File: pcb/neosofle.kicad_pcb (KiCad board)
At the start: 2 copper layers, 140.2 x 120 mm, 68 parts, among them J1 JST_ACH_BM02B-ACHSS-GAN-ETF_S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, SW1 CPG135001S30, SW10 CPG135001S30, SW11 CPG135001S30, SW12 CPG135001S30, SW13 CPG135001S30, SW14 CPG135001S30, SW15 CPG135001S30, SW16 CPG135001S30, SW17 CPG135001S30, SW18 CPG135001S30, SW19 CPG135001S30, SW2 CPG135001S30, SW20 CPG135001S30, SW21 CPG135001S30, SW22 CPG135001S30, SW23 CPG135001S30, SW24 CPG135001S30, SW25 RotaryEncoder_Switch, SW26 CPG135001S30, SW27 CPG135001S30, SW28 CPG135001S30, SW29 CPG135001S30, SW3 CPG135001S30, SW30 CPG135001S30, SW4 CPG135001S30, SW5 CPG135001S30, SW6 CPG135001S30, SW7 CPG135001S30, SW8 CPG135001S30, SW9 CPG135001S30, U1 nice!nano v2

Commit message: Update 3D model references, enlarge pads to hand solder JST connector.
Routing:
- net BAT+: track 61.7 -> 65.1 mm, vias 2 -> 3

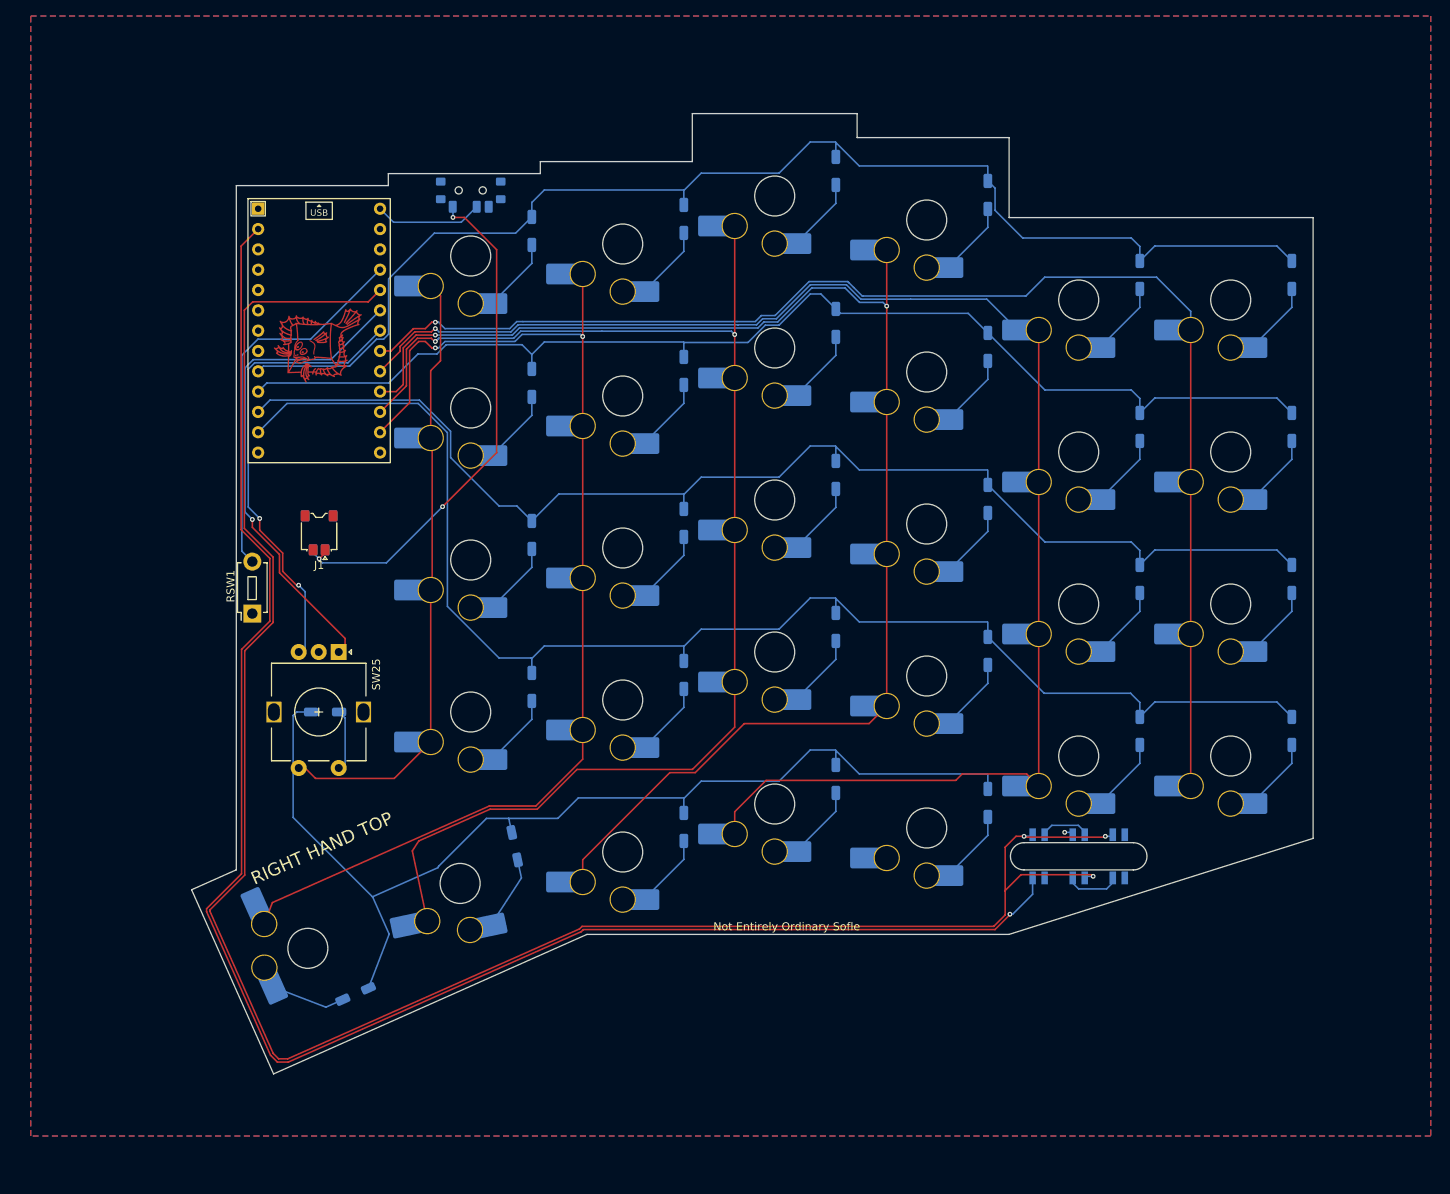
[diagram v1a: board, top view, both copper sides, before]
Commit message: Add 1u / 1.5u hybrid footprint for thumbkey, add teardrops, round tracks, add logo art and version text.
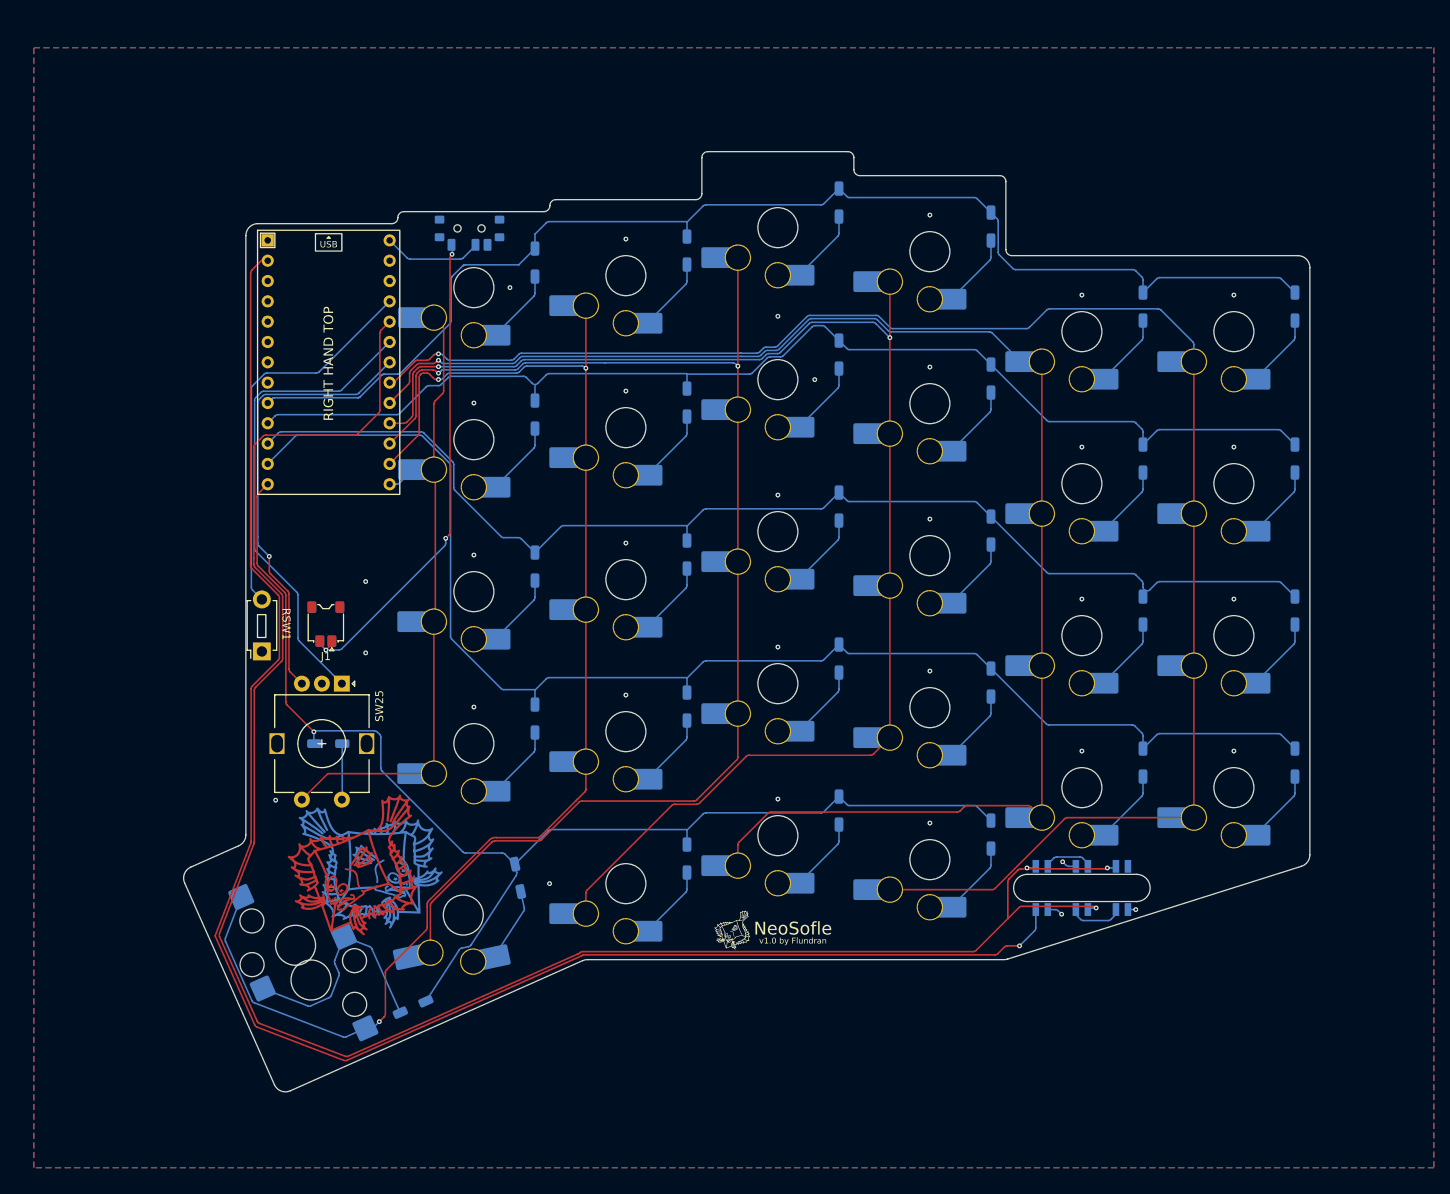
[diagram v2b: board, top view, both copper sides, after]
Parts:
- removed the G*** at (143.5, 108.0)
- added ?: , clipboard:a483b08f-474e-4f5d-84c2-fd1af38c265c, F.Cu at (201.9, 181.1)
- added G***: LOGO, NeoSofle:Logo_5mm, F.Cu at (195.6, 181.3)
- added G***: LOGO, NeoSofle:Logo_5mm, B.Cu at (210.3, 181.3)
- added REF**: LOGO, NeoSofle:Logo_16mm, F.Cu at (148.8, 173.7)
- added REF**: LOGO, NeoSofle:Logo_16mm, B.Cu at (150.1, 173.3)
- SW26: footprint NeoSofle:SW_Choc_V2_HS_CPG135001S30_1u -> NeoSofle:SW_Choc_V2_HS_CPG135001S30_1u1.5u_Hybrid
- moved J1 11.4 mm to (144.5, 142.8)
- moved D26 7.37 mm to (155.4, 190.6)
- moved RSW1 4.88 mm to (136.5, 146.2)
- moved PSW1 4.76 mm to (162.5, 93.3)
- moved U1 4.13 mm to (144.9, 110.1)
- moved D20 3.97 mm to (189.7, 153.1)
- moved SW6 3.97 mm to (258.0, 106.2)
- moved D6 3.97 mm to (265.7, 103.1)
- moved SW2 3.97 mm to (182.0, 99.2)
- moved SW29 3.97 mm to (201.0, 169.2)
- moved SW13 3.97 mm to (163.0, 138.7)
- moved D9 3.97 mm to (208.7, 109.1)
- moved SW11 3.97 mm to (239.0, 125.2)
- moved D29 3.97 mm to (208.7, 166.1)
- moved SW9 3.97 mm to (201.0, 112.2)
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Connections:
- net BAT+ renamed /BAT+
- net COL0 renamed /COL0
- net COL1 renamed /COL1
- net COL2 renamed /COL2
- net COL3 renamed /COL3
- net COL4 renamed /COL4
- net COL5 renamed /COL5
- net ENCA renamed /ENCA
- net ENCB renamed /ENCB
- net LED renamed /LED
- net ROW0 renamed /ROW0
- net ROW1 renamed /ROW1
- net ROW2 renamed /ROW2
- net ROW3 renamed /ROW3
- net ROW4 renamed /ROW4
- net RST renamed /RST
- net VBAT renamed /VBAT
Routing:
- net /COL0: track 167.6 -> 207.5 mm
- net /COL4: track 141.5 -> 168.4 mm, vias 2 -> 3
- net /ROW4: track 133.6 -> 157.3 mm, vias 0 -> 1
- net Net-(D26-A): track 9.41 -> 29.8 mm
- net +3.3V: track 249.4 -> 237.3 mm
- net /LED: track 213.7 -> 205.9 mm
- net /ROW2: track 155.1 -> 147.4 mm
- net /ROW3: track 174.8 -> 169.4 mm
- net /ROW0: track 161.0 -> 155.7 mm
- net /BAT+: track 65.1 -> 60.3 mm
- net GND: track 0.71 -> 4.71 mm, vias 1 -> 33
- net /COL3: track 169.1 -> 165.5 mm
- net /COL5: track 75.8 -> 77.7 mm
- net /ROW1: track 147.6 -> 146.1 mm
- net /VBAT: track 13.6 -> 12.5 mm
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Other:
- board size 140.2 x 120 mm -> 140.8 x 117.5 mm
- board text added: "NeoSofle"
- board text added: "v1.0 by Flundran"
- board text removed: "Not Entirely Ordinary Sofle"

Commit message: Improve logo art.
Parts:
- removed the G*** at (210.3, 181.3)
- added G***: LOGO, NeoSofle:Logo_6mm, B.Cu at (212.1, 181.5)
- G***: footprint NeoSofle:Logo_5mm -> NeoSofle:Logo_6mm
- REF** (x2): footprint NeoSofle:Logo_16mm -> NeoSofle:Logo_18mm
- moved REF** 0.86 mm to (149.4, 173.8), turned to 170 degrees
- moved G*** 0.85 mm to (196.4, 181.5), turned to 24 degrees
- moved REF** 0.42 mm to (149.1, 174.1), turned to 24 degrees
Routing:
- net GND: vias 33 -> 34
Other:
- board text added: "BOTTOM SIDE"
- board text added: "TOP SIDE"
- board text removed: "RIGHT HAND BACK"
- board text removed: "RIGHT HAND TOP"

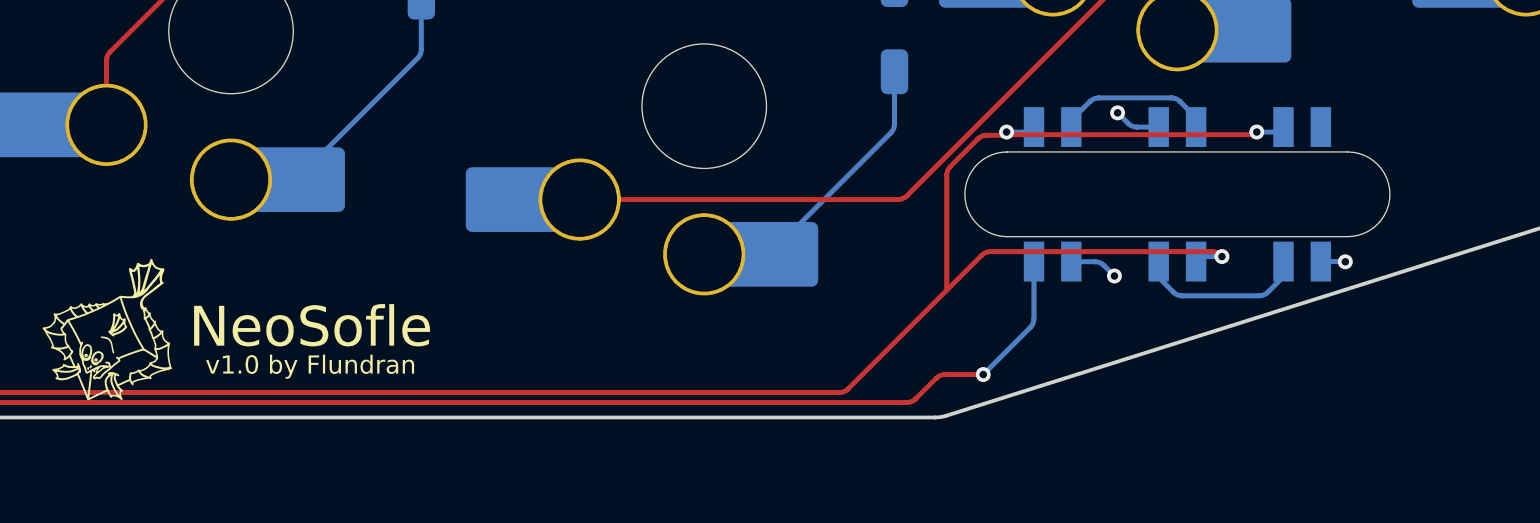
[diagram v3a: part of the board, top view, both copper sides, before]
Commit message: Fix minor DRC errors. Decrease width of LED cutout 0.1 mm.
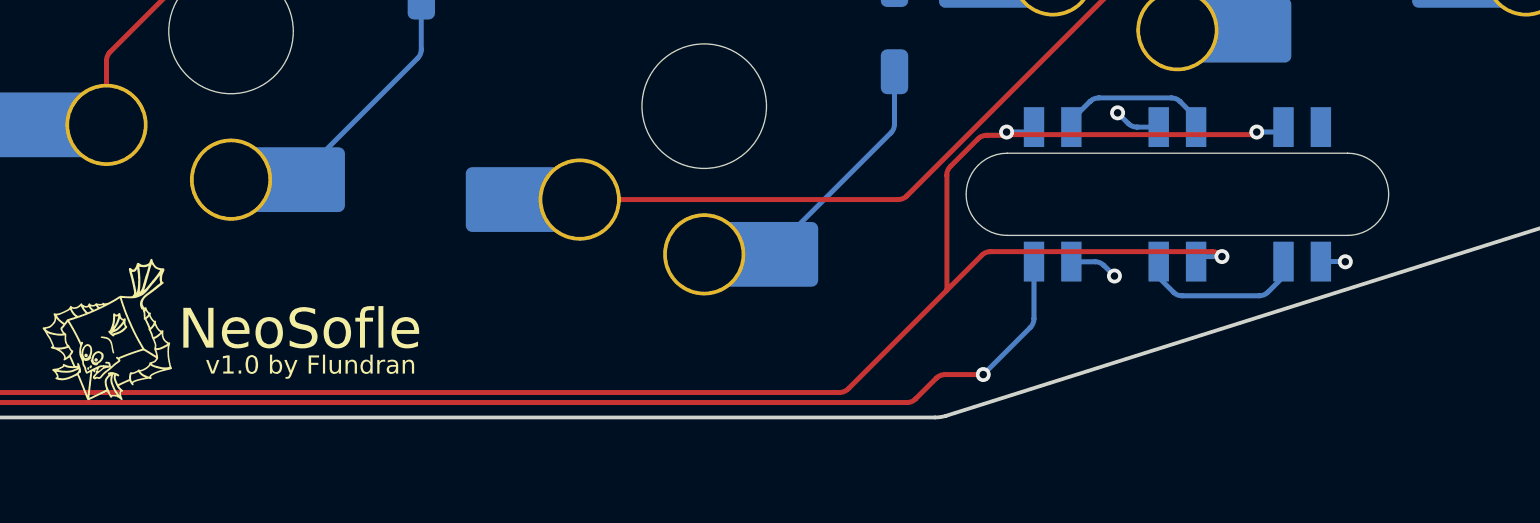
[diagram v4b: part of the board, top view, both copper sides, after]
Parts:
- removed ?: , clipboard:a483b08f-474e-4f5d-84c2-fd1af38c265c
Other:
- outline, holes or cut-outs redrawn

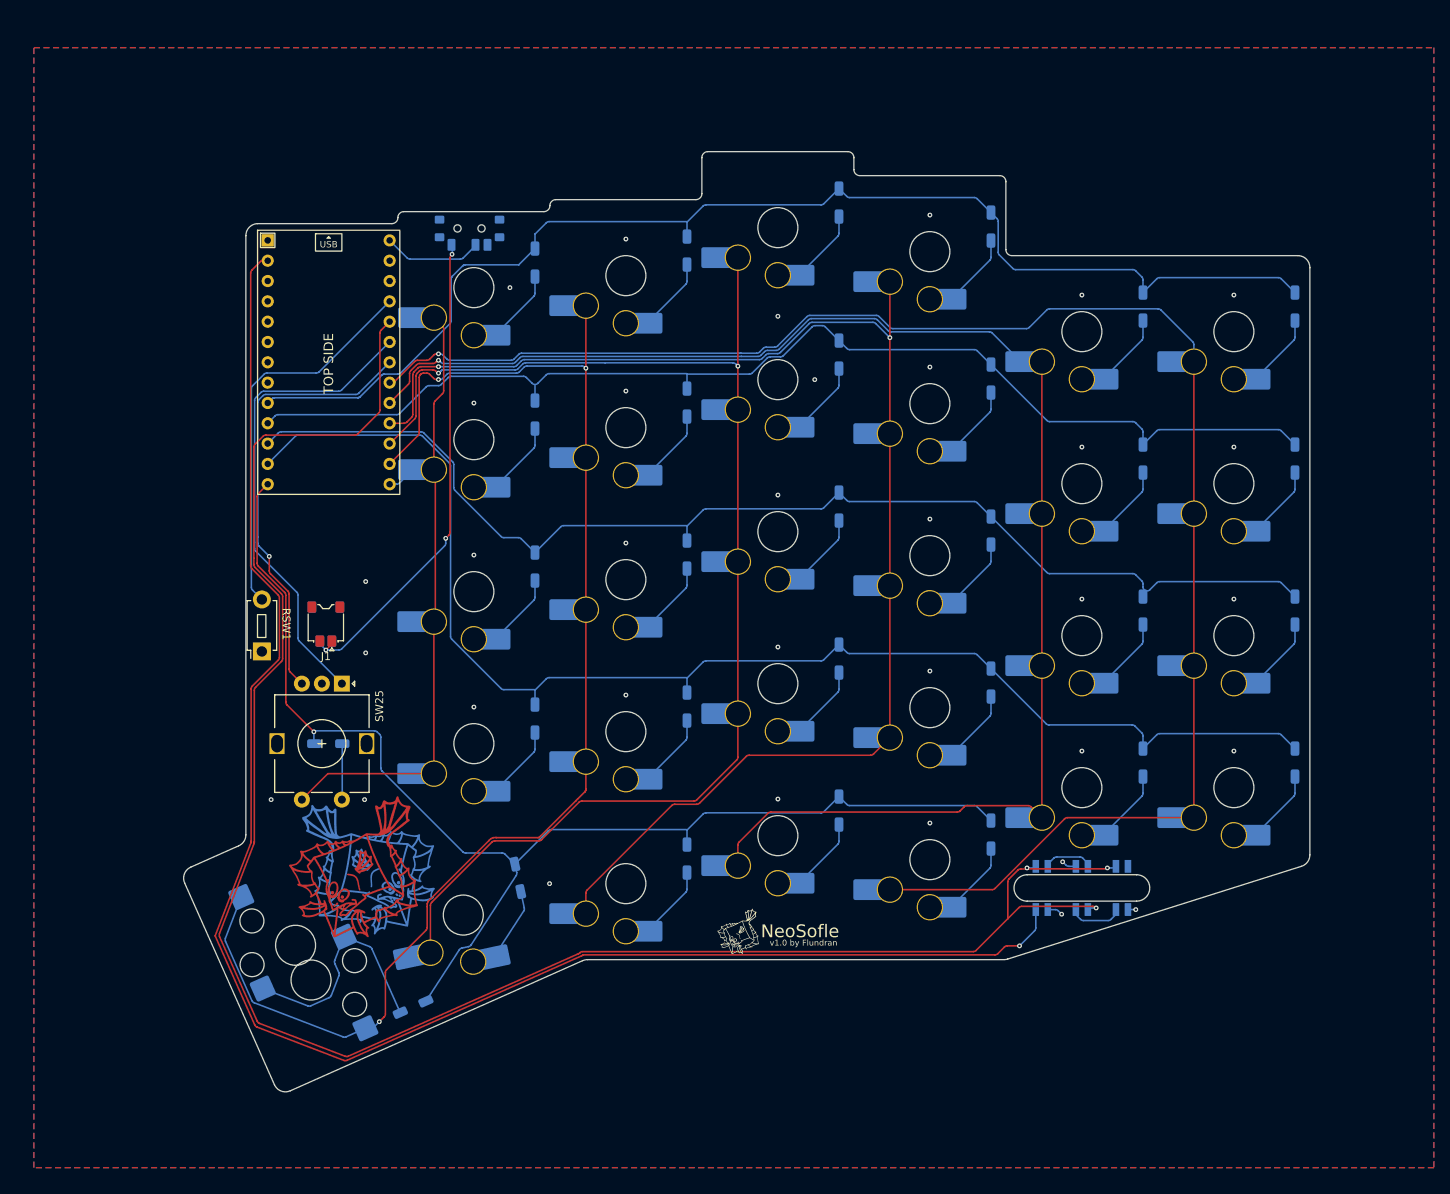
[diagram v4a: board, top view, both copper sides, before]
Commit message: Slightly resize board left edge. Multiple smaller fixes of silkscreen layer objects for JLC PCB DFM check, and similar. Add library version of NPTH choc footprint.
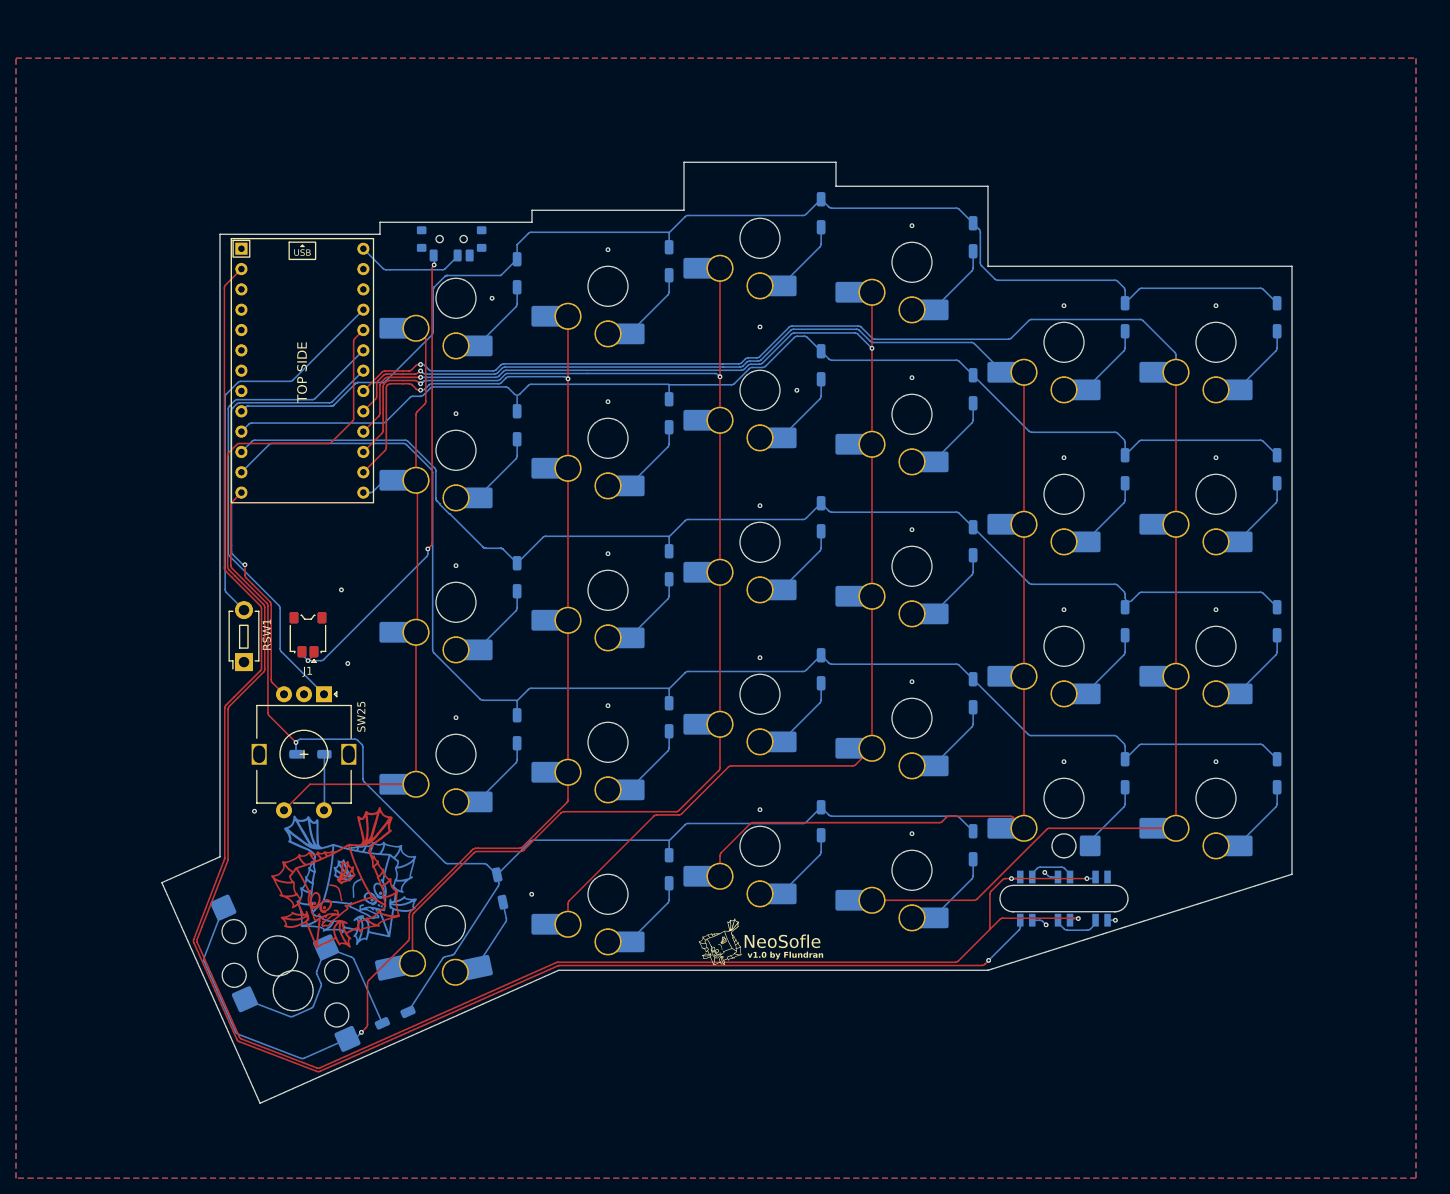
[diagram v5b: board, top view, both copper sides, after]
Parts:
- SW23: footprint NeoSofle:SW_Choc_V2_HS_CPG135001S30_1u -> NeoSofle:SW_Choc_V2_HS_CPG135001S30_1u_NPTH
- moved U1 3.45 mm to (141.6, 111.1)
- moved LED3 2.88 mm to (241.5, 177.1)
- moved SW6 2.60 mm to (255.8, 107.6)
- moved D29 2.60 mm to (206.4, 167.4)
- moved SW20 2.60 mm to (179.8, 157.6)
- moved SW1 2.60 mm to (160.8, 102.1)
- moved D21 2.60 mm to (206.4, 148.4)
- moved D27 2.60 mm to (166.3, 175.8)
- moved SW25 2.60 mm to (144.3, 151.6)
- moved SW23 2.60 mm to (236.8, 164.6)
- moved SW13 2.60 mm to (160.8, 140.1)
- moved D8 2.60 mm to (187.4, 116.4)
- moved SW26 2.60 mm to (138.5, 184.3)
- moved SW10 2.60 mm to (217.8, 116.6)
- moved SW17 2.60 mm to (236.8, 145.6)
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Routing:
- net /COL4: track 168.4 -> 171.6 mm
- net /ROW3: track 169.4 -> 171.0 mm
- net /ROW2: track 147.4 -> 148.9 mm
- net /COL0: track 207.5 -> 208.9 mm
- net +3.3V: track 237.3 -> 238.7 mm
- net /LED: track 205.9 -> 207.2 mm
- net /COL3: track 165.5 -> 166.8 mm
- net /COL1: track 185.7 -> 187.0 mm
- net /VBAT: track 12.5 -> 13.7 mm
- net /ROW4: track 157.3 -> 158.2 mm
- net /ROW0: track 155.7 -> 156.6 mm
- net /ROW1: track 146.1 -> 147.1 mm
- net /RST: track 48.7 -> 49.4 mm
- net /ENCA: track 59.8 -> 60.5 mm
- net /ENCB: track 55.9 -> 56.6 mm
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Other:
- board size 140.8 x 117.5 mm -> 141.3 x 117.6 mm
